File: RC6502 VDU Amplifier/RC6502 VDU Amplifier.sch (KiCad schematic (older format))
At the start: 10 parts, among them J1 Video, J2 Output, Q1 2N2222, Q2 2N2222

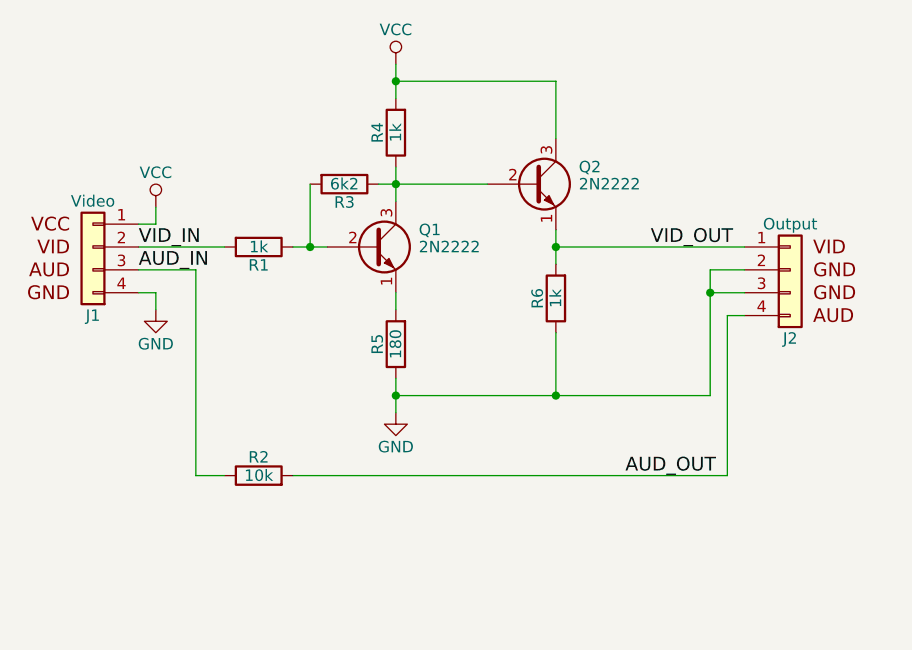
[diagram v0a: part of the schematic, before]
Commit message: VDU amplifier layout done
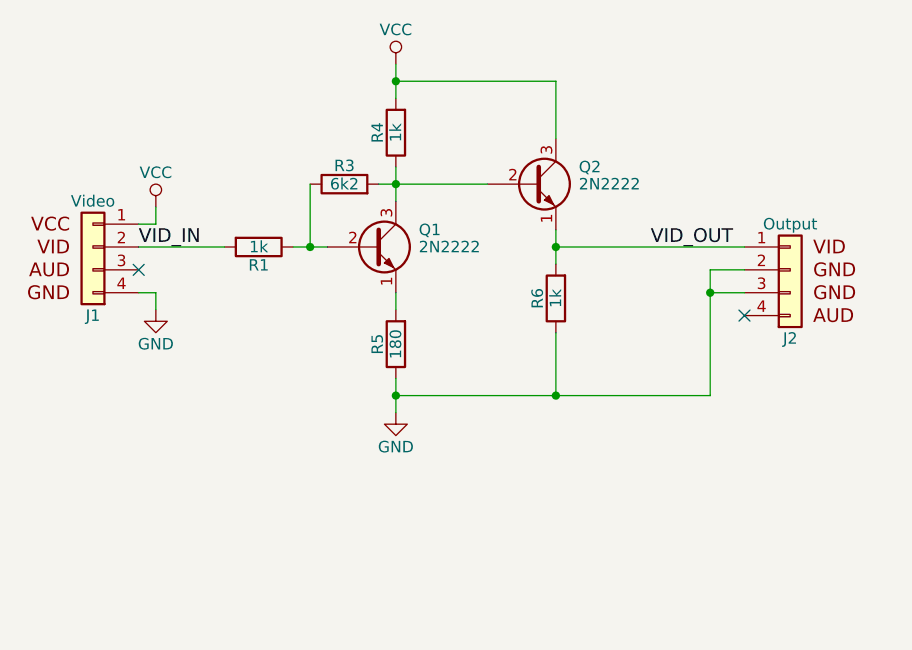
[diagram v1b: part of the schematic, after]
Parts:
- removed R2: 10k, Resistors_THT:R_Axial_DIN0207_L6.3mm_D2.5mm_P10.16mm_Horizontal, symbol R
- R1, R3, R4, R5, R6: footprint (none) -> Resistors_THT:R_Axial_DIN0207_L6.3mm_D2.5mm_P10.16mm_Horizontal
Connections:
- net at Q1.2 (B), R1.1: now also R3.1; no longer R3.2
- net at Q1.3 (C), Q2.2 (B), R4.1: now also R3.2; no longer R3.1
- net AUD_IN: no longer names the net of J1.3 (Pin_2)
- net AUD_OUT: no longer names the net of J2.4 (Pin_1)
- no-connect marks 0 -> 2
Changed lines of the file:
@@
 LIBS:contrib
 LIBS:valves
-LIBS:Composite Video Amplifier-cache
+LIBS:RC6502 VDU Amplifier-cache
 EELAYER 25 0
 EELAYER END
@@
 $EndComp
 $Comp
-L R R2
-U 1 1 5C338145
-P 4650 5050
-F 0 "R2" V 4730 5050 50  0000 C CNN
-F 1 "10k" V 4650 5050 50  0000 C CNN
-F 2 "Resistors_THT:R_Axial_DIN0207_L6.3mm_D2.5mm_P10.16mm_Horizontal" V 4580 5050 50  0001 C CNN
-F 3 "" H 4650 5050 50  0001 C CNN
-	1    4650 5050
-	0    -1   -1   0
-$EndComp
-$Comp
 L Output J2
 U 1 1 5C338146
@@
 Text Label 6725 4050 2    60   ~ 0
 VID_OUT
-Text Label 4125 4150 0    60   ~ 0
-AUD_IN
-Text Label 6650 5050 2    60   ~ 0
-AUD_OUT
 $Comp
 L Video J1
@@
 F 0 "R1" V 4730 4050 50  0000 C CNN
 F 1 "1k" V 4650 4050 50  0000 C CNN
-F 2 "" V 4580 4050 50  0001 C CNN
+F 2 "Resistors_THT:R_Axial_DIN0207_L6.3mm_D2.5mm_P10.16mm_Horizontal" V 4580 4050 50  0001 C CNN
 F 3 "" H 4650 4050 50  0001 C CNN
 	1    4650 4050
@@
 F 0 "R5" V 5330 4475 50  0000 C CNN
 F 1 "180" V 5250 4475 50  0000 C CNN
-F 2 "" V 5180 4475 50  0001 C CNN
+F 2 "Resistors_THT:R_Axial_DIN0207_L6.3mm_D2.5mm_P10.16mm_Horizontal" V 5180 4475 50  0001 C CNN
 F 3 "" H 5250 4475 50  0001 C CNN
 	1    5250 4475
@@
 F 0 "R3" V 5105 3775 50  0000 C CNN
 F 1 "6k2" V 5025 3775 50  0000 C CNN
-F 2 "" V 4955 3775 50  0001 C CNN
+F 2 "Resistors_THT:R_Axial_DIN0207_L6.3mm_D2.5mm_P10.16mm_Horizontal" V 4955 3775 50  0001 C CNN
 F 3 "" H 5025 3775 50  0001 C CNN
 	1    5025 3775
-	0    1    1    0
+	0    -1   -1   0
 $EndComp
 $Comp
@@
 F 0 "R4" V 5330 3550 50  0000 C CNN
 F 1 "1k" V 5250 3550 50  0000 C CNN
-F 2 "" V 5180 3550 50  0001 C CNN
+F 2 "Resistors_THT:R_Axial_DIN0207_L6.3mm_D2.5mm_P10.16mm_Horizontal" V 5180 3550 50  0001 C CNN
 F 3 "" H 5250 3550 50  0001 C CNN
 	1    5250 3550
@@
 F 0 "R6" V 6030 4275 50  0000 C CNN
 F 1 "1k" V 5950 4275 50  0000 C CNN
-F 2 "" V 5880 4275 50  0001 C CNN
+F 2 "Resistors_THT:R_Axial_DIN0207_L6.3mm_D2.5mm_P10.16mm_Horizontal" V 5880 4275 50  0001 C CNN
 F 3 "" H 5950 4275 50  0001 C CNN
 	1    5950 4275
@@
 	6625 4150 6775 4150
 Wire Wire Line
-	4125 4150 4375 4150
-Wire Wire Line
-	4375 4150 4375 5050
-Wire Wire Line
 	6625 4700 6625 4150
 Wire Wire Line
 	6775 4250 6625 4250
 Connection ~ 6625 4250
-Wire Wire Line
-	6775 4350 6700 4350
-Wire Wire Line
-	6700 4350 6700 5050
 Wire Wire Line
 	4500 4050 4125 4050
@@
 Connection ~ 5950 4700
 Wire Wire Line
-	4375 5050 4500 5050
-Wire Wire Line
 	5250 4250 5250 4325
 Wire Wire Line
 	5250 3325 5950 3325
-Wire Wire Line
-	6700 5050 4800 5050
 Text Notes 7025 6850 0    60   ~ 0
 This is the analog video amplification circuit used with the VDU card, this variant is\nbased on the original schematic found in the book "22 Micro-computer projects: To\nbuild, use and learn" by Daniel Metzger. An excellent book if you can find a copy!
 Text Notes 7350 7500 0    60   ~ 0
 Video amplifier for the RC6502 VDU
+NoConn ~ 6775 4350
+NoConn ~ 4125 4150
 $EndSCHEMATC
